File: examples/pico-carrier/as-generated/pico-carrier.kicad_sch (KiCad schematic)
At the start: 9 parts, among them J1 5V IN, J3 GP0-GP15, J4 GP16-GP28, PWR, U1 Pico

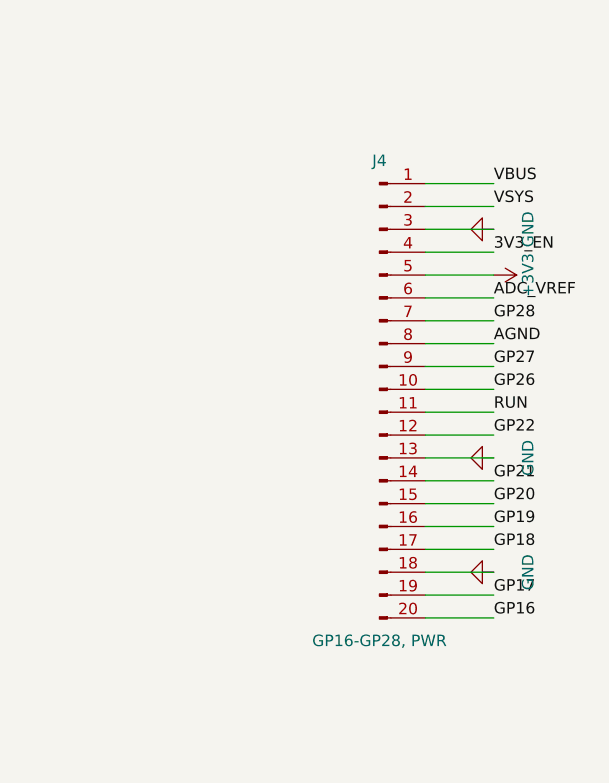
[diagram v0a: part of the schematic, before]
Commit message: Route the sheets, and anchor the ground vias where the loop is
The user's verdict on the last round stood: none of the five schematics
read as a human drawing, and the artwork still had its physics wrong.
This round answers both.

The schematic side replaces the stub-and-label sheet with a router.
Every signal net becomes a tree of straight, L-, Z- and detour-shaped
runs on the 1.27 mm grid: legs leave a pin along its own stub, escape
distances stagger so a bus does not fight over one column, every pin
reserves a runway another wire may cross but not ride along, and the
sheet frame, title block and notes are obstacles like any symbol.
Fragments merge Kruskal-style so a rail whose regulator is boxed in
still gets its capacitors chained; each surviving fragment keeps one
label, because the label is what names the net. Collinear same-net
segments are unioned and then split at every tee - KiCad 9's
connectivity requires files drawn the way the editor draws them, with
a junction dot and a wire break wherever a branch tees in, and a wire
that runs through a junction connects on one side of it only. That
last fact cost an evening and is now a comment.

Trying to draw the wires found what no rule had: the buck's LED was
upside down with its ground pointing up into the resistor above it,
both breakout headers faced away from everything they connect to
(fixed with mirrored symbols, which Part now supports), the FPGA
sheet's notes printed over the 1.2 V regulator, and its programming
header sat inside the title block. Wired: buck, motor and op-amp
completely; the Pico carrier 31 of 33 nets; the FPGA board 16 of 19 -
what stays labelled is what a human would label too.

The artwork side anchors every FPGA decoupling capacitor's ground via
against its own pad, on the far side from the supply pad, with the
1.2 mm stub as the whole loop - retiring all seven
layout.decoupling_via findings and that waiver with them. A back_cost
experiment (0.4 to 0.6) to shrink the return-path cuts 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
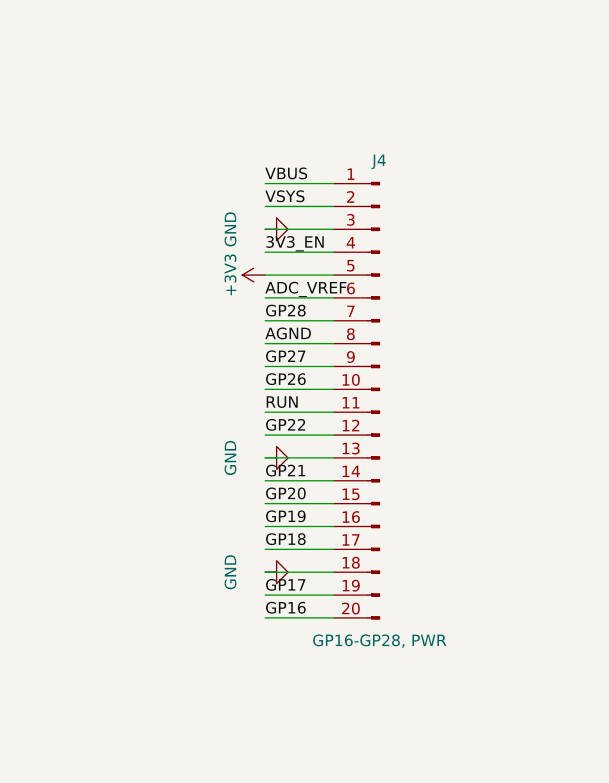
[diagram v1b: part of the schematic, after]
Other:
- moved on the sheet: J4

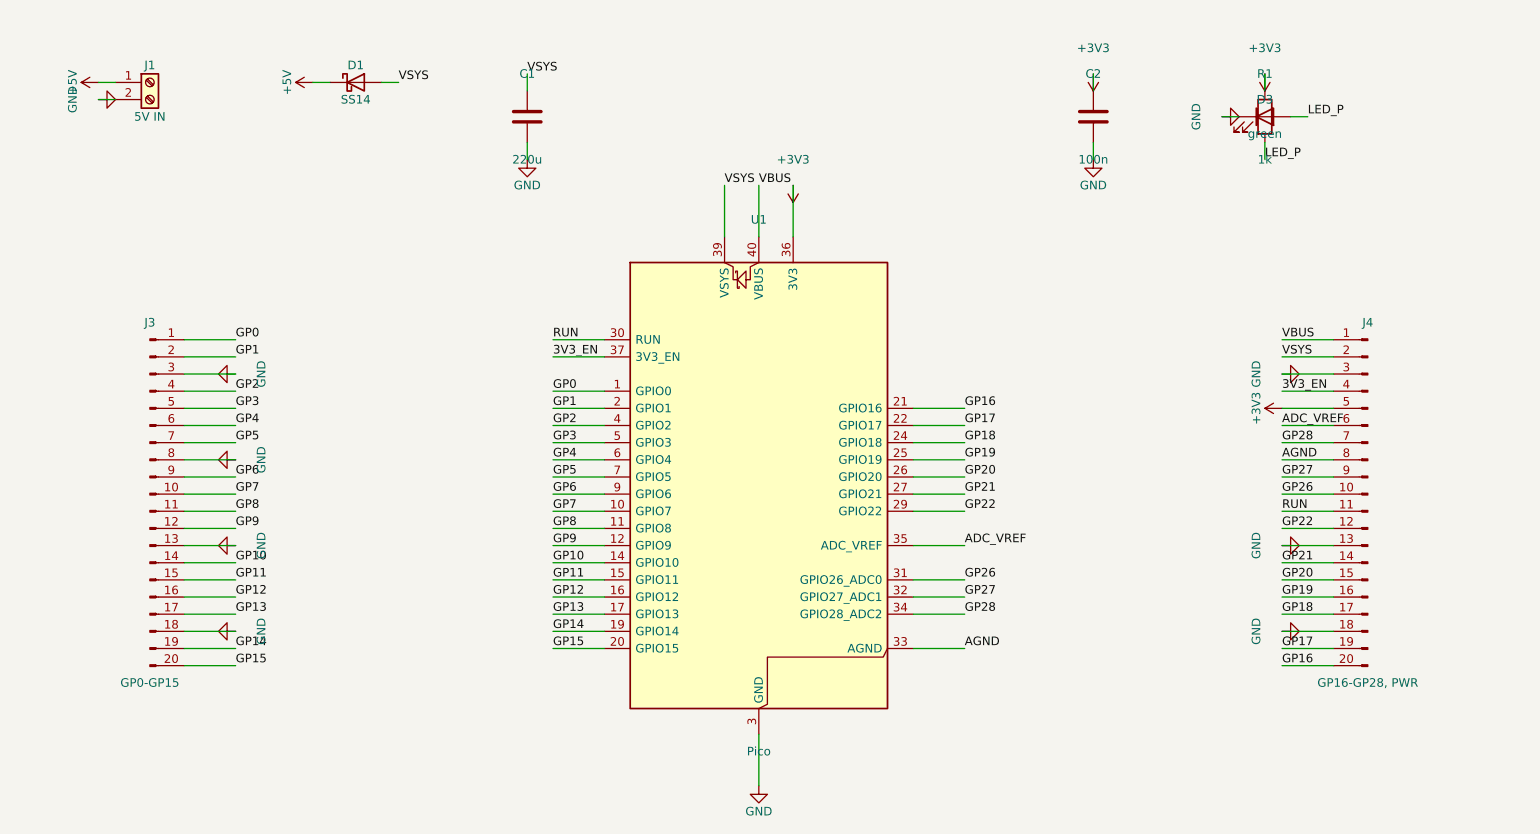
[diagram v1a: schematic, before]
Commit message: Regenerate the five with stitched pours, silk that speaks, and wires that never double back
All ten variants rebuilt by the fixed generator: reviewed boards carry
ground on both faces with the stitching ring (buck 35 vias, fpga 116),
thru_hole_only front pours, the board id and connector pin names in
silk, and the buck's explicit ground return; the sheets hook power up
through upright symbols and source-anchored flags with no overlapping
wires and no junction-less tees left. Every reviewed variant passes its
own gate with zero errors; every as-generated variant still fails, now
also for the rules this round added.

Co-Authored-By: Claude Fable 5 <noreply@anthropic.com>
Claude-Session: https://claude.ai/code/session_01DUj7Ltu92tWg159mCSacwY
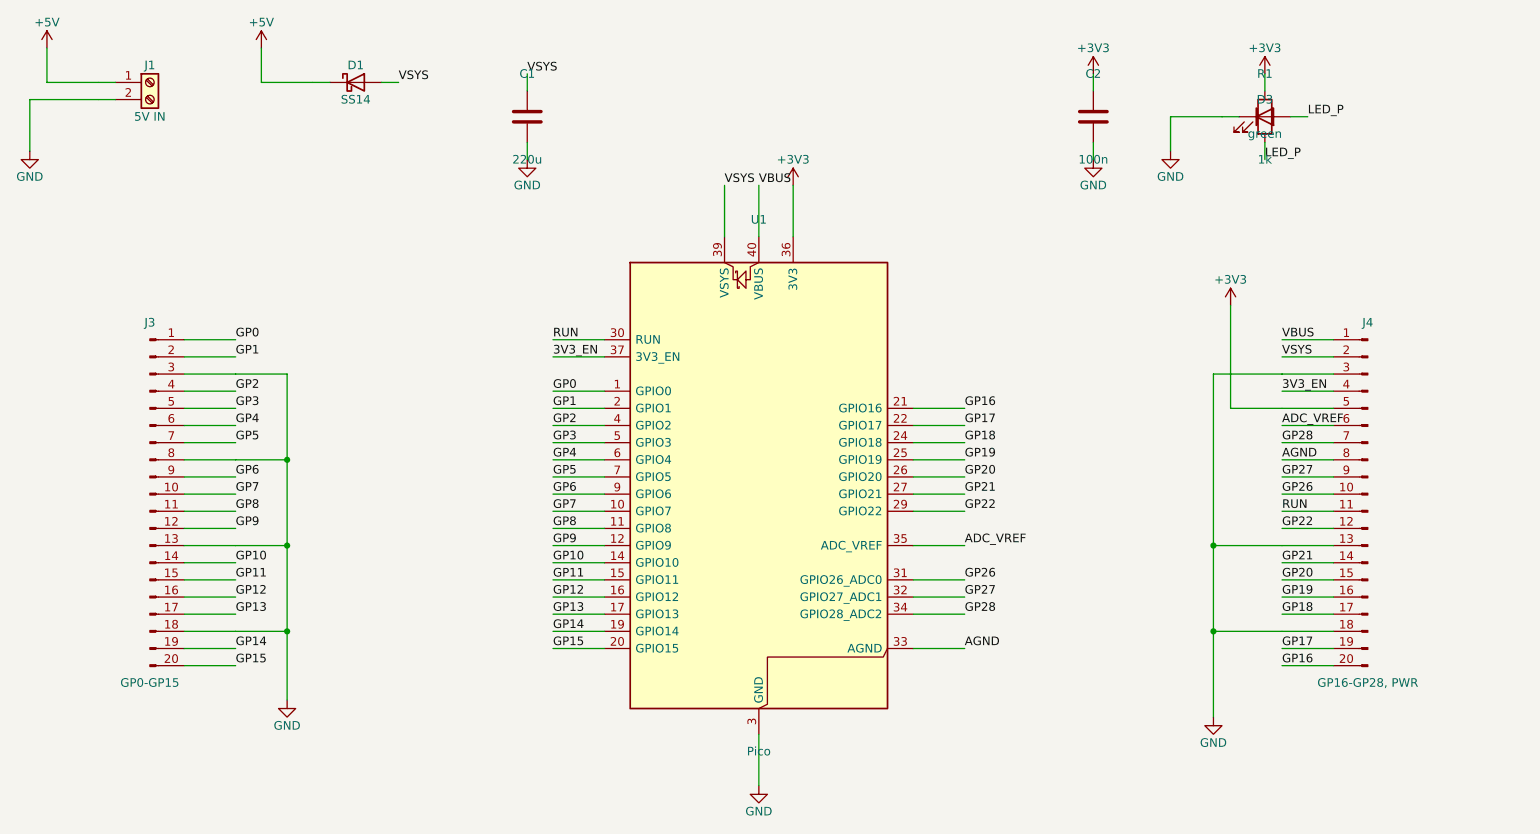
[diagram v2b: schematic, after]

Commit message: Regenerate the five as round three drew them
All five reviewed projects pass their gates again: the buck all wire
with its feedback drawn home, the motor's logic named at the header,
the carrier reading as the pinout table it is - with its feed diode
finally pointing the right way - the filter compact with test points,
and the FPGA's capacitors sitting beside the units they feed. Thirty
renders redrawn, verdict tables at today's numbers.

Co-Authored-By: Claude Fable 5 <noreply@anthropic.com>
Claude-Session: https://claude.ai/code/session_01DUj7Ltu92tWg159mCSacwY
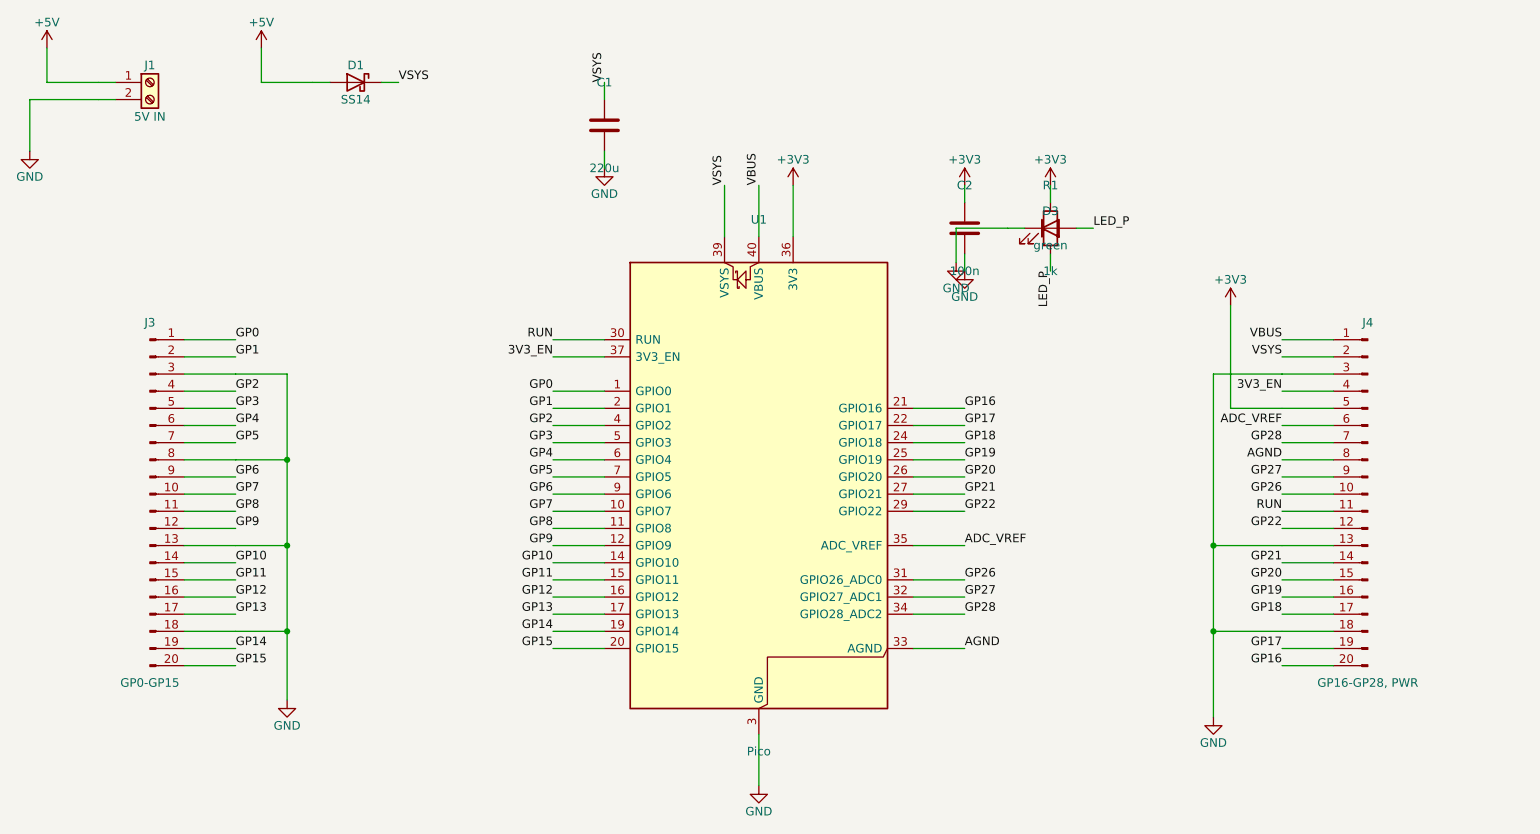
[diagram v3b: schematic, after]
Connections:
- net +5V: now also D1.2 (A); no longer D1.1 (K)
- net VSYS: now also D1.1 (K); no longer D1.2 (A)
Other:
- moved on the sheet: C1, C2, D3, R1

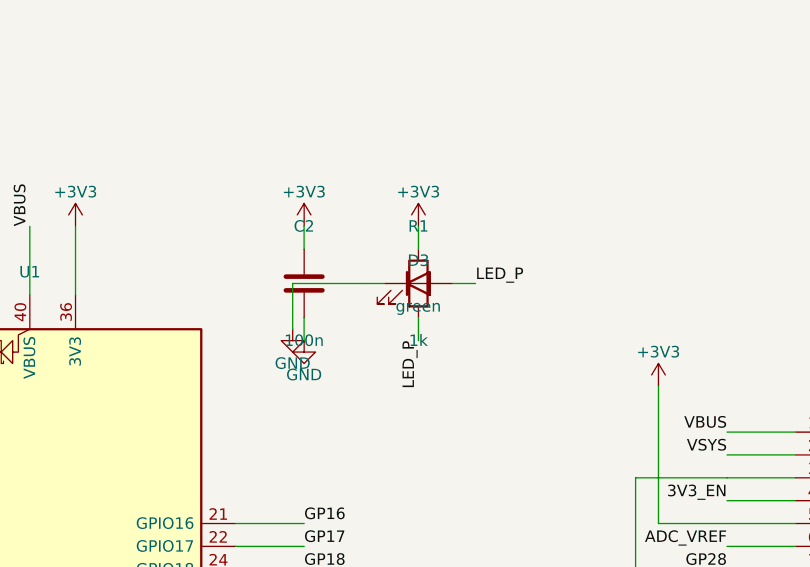
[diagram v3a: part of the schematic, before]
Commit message: Regenerate the four boards round four has settled
The buck, the motor driver, the carrier and the filter as the current
generator draws them: interior ground stitching on all four, the motor
driver's bundle tight and its board twelve millimetres shorter, the
filter compact and hand-placed, the carrier's indicator in a column of
its own. All four pass their gates. The FPGA is still regenerating.

Co-Authored-By: Claude Fable 5 <noreply@anthropic.com>
Claude-Session: https://claude.ai/code/session_01DUj7Ltu92tWg159mCSacwY
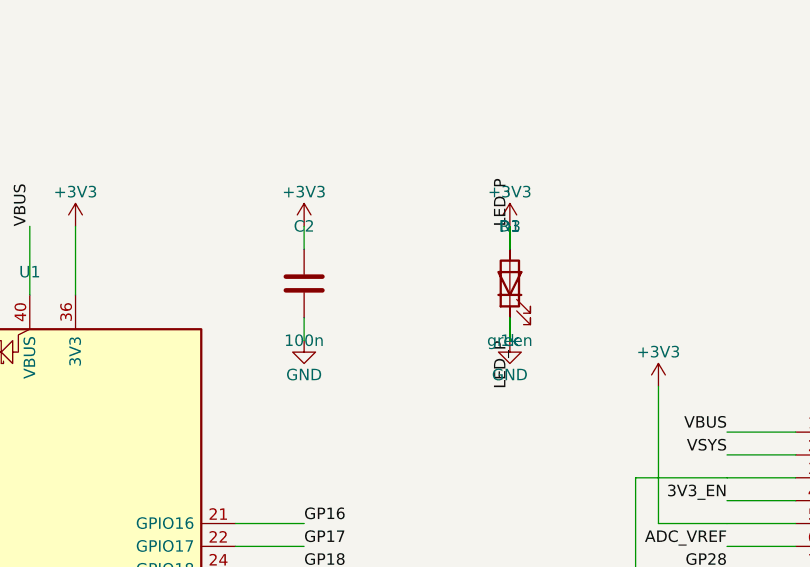
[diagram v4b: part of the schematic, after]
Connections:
- net GND is gone; now on net +3V3: C1.2, C2.2, D3.1 (K), J1.2 (Pin_2), J3.13 (Pin_13), J3.18 (Pin_18), J3.3 (Pin_3), J3.8 (Pin_8), J4.13 (Pin_13), J4.18 (Pin_18), J4.3 (Pin_3), U1.13 (GND), U1.18 (GND), U1.23 (GND), U1.28 (GND), U1.3 (GND), U1.38 (GND), U1.8 (GND)
- net LED_P is gone; now on net +3V3: D3.2 (A), R1.2
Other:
- moved on the sheet: D3, R1
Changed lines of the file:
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@@
     (instances (project "pico-carrier" (path "/f86b03a2-2f64-5dc5-a6a7-b575bc25ae3a" (reference "C2") (unit 1))))
   )
-  (wire (pts (xy 193.35 56.96) (xy 193.35 54.42)) (stroke (width 0) (type default)))
-  (wire (pts (xy 193.35 64.58) (xy 193.35 67.12)) (stroke (width 0) (type default)))
-  (label "LED_P" (at 193.35 67.12 90) (effects (font (size 1.27 1.27)) (justify right bottom)))
-  (symbol (lib_id "Device:R") (at 193.35 60.77 0.0) (unit 1)
+  (wire (pts (xy 203.51 56.96) (xy 203.51 54.42)) (stroke (width 0) (type default)))
+  (wire (pts (xy 203.51 64.58) (xy 203.51 67.12)) (stroke (width 0) (type default)))
+  (label "LED_P" (at 203.51 67.12 90) (effects (font (size 1.27 1.27)) (justify right bottom)))
+  (symbol (lib_id "Device:R") (at 203.51 60.77 0.0) (unit 1)
     (exclude_from_sim no) (in_bom yes) (on_board yes) (dnp no)
-    (property "Reference" "R1" (at 193.35 54.42 0) (effects (font (size 1.27 1.27))))
-    (property "Value" "1k" (at 193.35 67.12 0) (effects (font (size 1.27 1.27))))
-    (property "Footprint" "Resistor_SMD:R_0805_2012Metric" (at 193.35 60.77 0) (effects (font (size 1.27 1.27)) hide))
-    (property "Datasheet" "https://www.yageo.com/upload/media/product/productsearch/datasheet/rchip/PYu-RC_Group_51_RoHS_L_12.pdf" (at 193.35 60.77 0) (effects (font (size 1.27 1.27)) hide))
+    (property "Reference" "R1" (at 203.51 54.42 0) (effects (font (size 1.27 1.27))))
+    (property "Value" "1k" (at 203.51 67.12 0) (effects (font (size 1.27 1.27))))
+    (property "Footprint" "Resistor_SMD:R_0805_2012Metric" (at 203.51 60.77 0) (effects (font (size 1.27 1.27)) hide))
+    (property "Datasheet" "https://www.yageo.com/upload/media/product/productsearch/datasheet/rchip/PYu-RC_Group_51_RoHS_L_12.pdf" (at 203.51 60.77 0) (effects (font (size 1.27 1.27)) hide))
     (pin "1" (uuid "18e2316f-fad8-538b-94a2-1adbf40006ad-p1"))
     (pin "2" (uuid "18e2316f-fad8-538b-94a2-1adbf40006ad-p2"))
     (instances (project "pico-carrier" (path "/f86b03a2-2f64-5dc5-a6a7-b575bc25ae3a" (reference "R1") (unit 1))))
   )
-  (wire (pts (xy 189.54 60.77) (xy 187.0 60.77)) (stroke (width 0) (type default)))
-  (wire (pts (xy 197.16 60.77) (xy 199.7 60.77)) (stroke (width 0) (type default)))
-  (label "LED_P" (at 199.7 60.77 0) (effects (font (size 1.27 1.27)) (justify left bottom)))
-  (symbol (lib_id "Device:LED") (at 193.35 60.77 0.0) (unit 1)
+  (wire (pts (xy 203.51 64.58) (xy 203.51 67.12)) (stroke (width 0) (type default)))
+  (wire (pts (xy 203.51 56.96) (xy 203.51 54.42)) (stroke (width 0) (type default)))
+  (label "LED_P" (at 203.51 54.42 90) (effects (font (size 1.27 1.27)) (justify left bottom)))
+  (symbol (lib_id "Device:LED") (at 203.51 60.77 90.0) (unit 1)
     (exclude_from_sim no) (in_bom yes) (on_board yes) (dnp no)
-    (property "Reference" "D3" (at 193.35 58.23 0) (effects (font (size 1.27 1.27))))
-    (property "Value" "green" (at 193.35 63.31 0) (effects (font (size 1.27 1.27))))
-    (property "Footprint" "LED_SMD:LED_0805_2012Metric" (at 193.35 60.77 0) (effects (font (size 1.27 1.27)) hide))
-    (property "Datasheet" "https://optoelectronics.liteon.com/upload/download/DS-22-98-0002/LTST-C170KGKT.pdf" (at 193.35 60.77 0) (effects (font (size 1.27 1.27)) hide))
+    (property "Reference" "D3" (at 203.51 54.42 90) (effects (font (size 1.27 1.27))))
+    (property "Value" "green" (at 203.51 67.12 90) (effects (font (size 1.27 1.27))))
+    (property "Footprint" "LED_SMD:LED_0805_2012Metric" (at 203.51 60.77 0) (effects (font (size 1.27 1.27)) hide))
+    (property "Datasheet" "https://optoelectronics.liteon.com/upload/download/DS-22-98-0002/LTST-C170KGKT.pdf" (at 203.51 60.77 0) (effects (font (size 1.27 1.27)) hide))
     (pin "1" (uuid "634a87af-8e5f-58bb-80cb-050cf18f78ba-p1"))
     (pin "2" (uuid "634a87af-8e5f-58bb-80cb-050cf18f78ba-p2"))
@@
   (wire (pts (xy 84.13 39.18) (xy 76.51 39.18)) (stroke (width 0) (type default)))
   (wire (pts (xy 76.51 34.1) (xy 76.51 39.18)) (stroke (width 0) (type default)))
-  (wire (pts (xy 187.0 60.77) (xy 179.38 60.77)) (stroke (width 0) (type default)))
-  (wire (pts (xy 179.38 60.77) (xy 179.38 65.85)) (stroke (width 0) (type default)))
   (symbol (lib_id "power:GND") (at 150.17 143.32 0) (unit 1)
     (exclude_from_sim no) (in_bom no) (on_board yes) (dnp no)
@@
     (instances (project "pico-carrier" (path "/f86b03a2-2f64-5dc5-a6a7-b575bc25ae3a" (reference "#PWR11") (unit 1))))
   )
-  (symbol (lib_id "power:+3V3") (at 193.35 54.42 0) (unit 1)
+  (symbol (lib_id "power:+3V3") (at 203.51 54.42 0) (unit 1)
     (exclude_from_sim no) (in_bom no) (on_board yes) (dnp no)
-    (property "Reference" "#PWR12" (at 193.35 54.42 0) (effects (font (size 1.27 1.27)) hide))
-    (property "Value" "+3V3" (at 193.35 50.61 0) (effects (font (size 1.27 1.27))))
-    (property "Footprint" "" (at 193.35 54.42 0) (effects (font (size 1.27 1.27)) hide))
-    (property "Datasheet" "" (at 193.35 54.42 0) (effects (font (size 1.27 1.27)) hide))
+    (property "Reference" "#PWR12" (at 203.51 54.42 0) (effects (font (size 1.27 1.27)) hide))
+    (property "Value" "+3V3" (at 203.51 50.61 0) (effects (font (size 1.27 1.27))))
+    (property "Footprint" "" (at 203.51 54.42 0) (effects (font (size 1.27 1.27)) hide))
+    (property "Datasheet" "" (at 203.51 54.42 0) (effects (font (size 1.27 1.27)) hide))
     (pin "1" (uuid "7510f3a5-d161-569e-ae8b-ba7e4d86b452-p"))
     (instances (project "pico-carrier" (path "/f86b03a2-2f64-5dc5-a6a7-b575bc25ae3a" (reference "#PWR12") (unit 1))))
   )
-  (symbol (lib_id "power:GND") (at 179.38 65.85 0) (unit 1)
+  (symbol (lib_id "power:GND") (at 203.51 67.12 0) (unit 1)
     (exclude_from_sim no) (in_bom no) (on_board yes) (dnp no)
-    (property "Reference" "#PWR13" (at 179.38 65.85 0) (effects (font (size 1.27 1.27)) hide))
-    (property "Value" "GND" (at 179.38 69.66 0) (effects (font (size 1.27 1.27))))
-    (property "Footprint" "" (at 179.38 65.85 0) (effects (font (size 1.27 1.27)) hide))
-    (property "Datasheet" "" (at 179.38 65.85 0) (effects (font (size 1.27 1.27)) hide))
+    (property "Reference" "#PWR13" (at 203.51 67.12 0) (effects (font (size 1.27 1.27)) hide))
+    (property "Value" "GND" (at 203.51 70.93 0) (effects (font (size 1.27 1.27))))
+    (property "Footprint" "" (at 203.51 67.12 0) (effects (font (size 1.27 1.27)) hide))
+    (property "Datasheet" "" (at 203.51 67.12 0) (effects (font (size 1.27 1.27)) hide))
     (pin "1" (uuid "bd382a54-694d-5007-a758-46e341ab7157-p"))
     (instances (project "pico-carrier" (path "/f86b03a2-2f64-5dc5-a6a7-b575bc25ae3a" (reference "#PWR13") (unit 1))))
